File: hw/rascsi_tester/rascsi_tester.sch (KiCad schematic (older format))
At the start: 16 parts, among them J1 USB_B_Micro, J2 Conn_02x25_Odd_Even, J3 Conn_01x02_Male, J4 L717SDB25PA4CH4F, X1 Mac, X2 Dogcow, X3 Mac2, X4 Raspberry Pi, X5 Dogcow2, X6 Mac Trashcan, X7 Pi, X8 Pi

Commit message: Updated tester board
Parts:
- removed X6: Mac Trashcan, SamacSys_Parts:mac_trashcan, symbol SamacSys_Parts:Logo
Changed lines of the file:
@@
-$EndComp
-$Comp
-L SamacSys_Parts:Logo X6
-U 1 1 5EFCDFAD
-P 8650 4200
-F 0 "X6" H 8500 4300 50  0000 L CNN
-F 1 "Mac Trashcan" H 8700 4300 50  0000 L CNN
-F 2 "SamacSys_Parts:mac_trashcan" H 8650 4200 50  0001 C CNN
-F 3 "" H 8650 4200 50  0001 C CNN
-	1    8650 4200
-	1    0    0    -1
 $EndComp
 $Comp

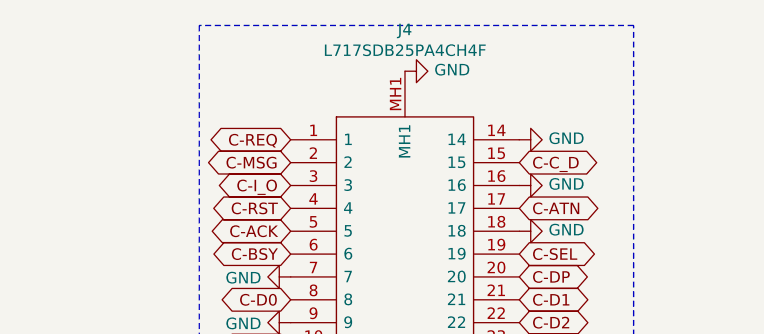
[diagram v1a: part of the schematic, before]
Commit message: Cleanup LCSC part number, regenerate gerbers and re-generate schematics
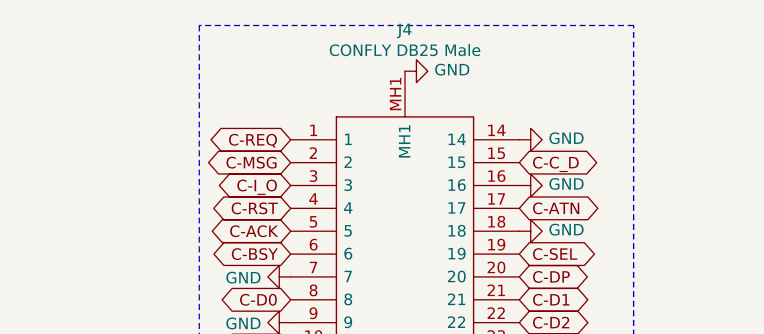
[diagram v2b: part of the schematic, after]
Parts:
- J2: LCSC (none) -> C40024
- J4: value L717SDB25PA4CH4F -> CONFLY DB25 Male; LCSC (none) -> C75751
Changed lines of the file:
@@
 EESchema Schematic File Version 4
+LIBS:rascsi_tester-cache
 EELAYER 30 0
 EELAYER END
@@
 F 2 "Connector_PinHeader_2.54mm:PinHeader_2x25_P2.54mm_Vertical" H 2250 2850 50  0001 C CNN
 F 3 "~" H 2250 2850 50  0001 C CNN
+F 4 "C40024" H 2250 2850 50  0001 C CNN "LCSC"
 	1    2250 2850
 	0    -1   -1   0
@@
 P 8750 800
 F 0 "J4" V 8569 800 50  0000 C CNN
-F 1 "L717SDB25PA4CH4F" V 8660 800 50  0000 C CNN
+F 1 "CONFLY DB25 Male" V 8660 800 50  0000 C CNN
 F 2 "L717SDB25PA4CH4F" H 10400 1100 50  0001 L CNN
 F 3 "https://componentsearchengine.com/Datasheets/1/L717SDB25PA4CH4F.pdf" H 10400 1000 50  0001 L CNN
@@
 F 8 "Amphenol" H 10400 500 50  0001 L CNN "Manufacturer_Name"
 F 9 "L717SDB25PA4CH4F" H 10400 400 50  0001 L CNN "Manufacturer_Part_Number"
+F 10 "C75751" V 8750 800 50  0001 C CNN "LCSC"
 	1    8750 800
 	0    -1   1    0
